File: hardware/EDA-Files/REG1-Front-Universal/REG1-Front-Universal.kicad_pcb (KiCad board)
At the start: 2 copper layers, 15.7 x 43 mm, 10 parts, among them J1 Conn_02x04_Odd_Even, SW1 Prog, SW2 Func, SW5 Res, SW6 BL

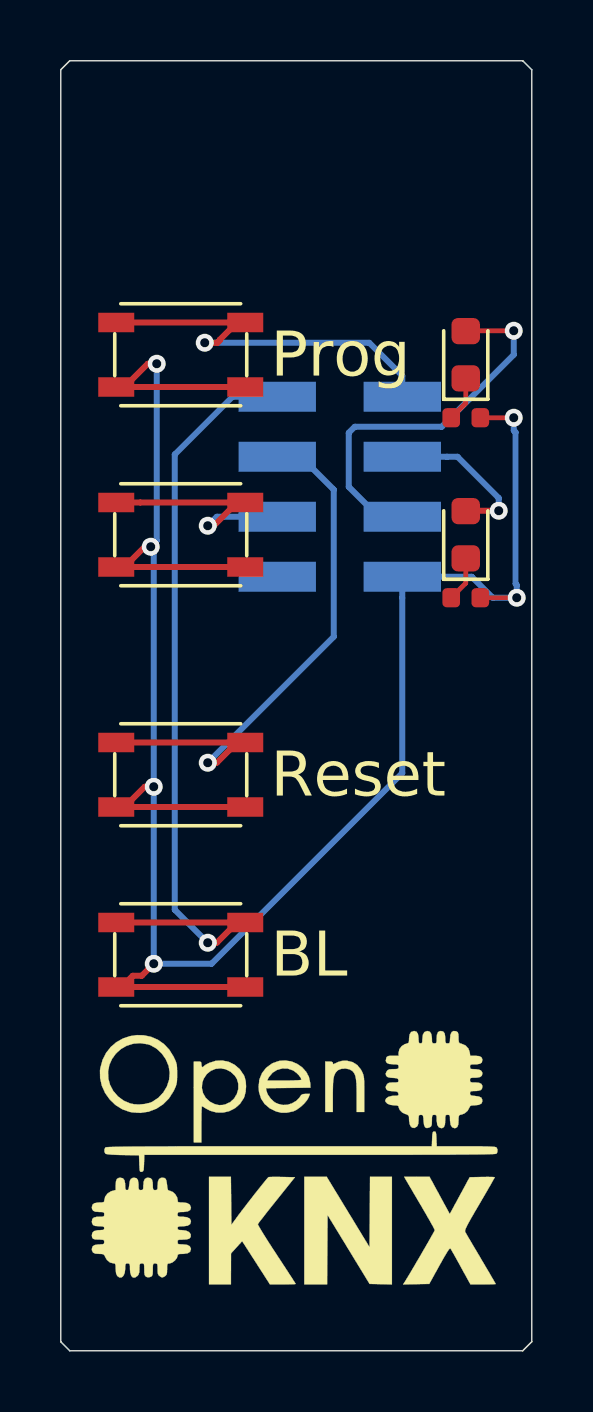
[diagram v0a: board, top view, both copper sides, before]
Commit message: rotate connector, rotate switches, 0.2mm smaller on each side, corrected pinout of connector
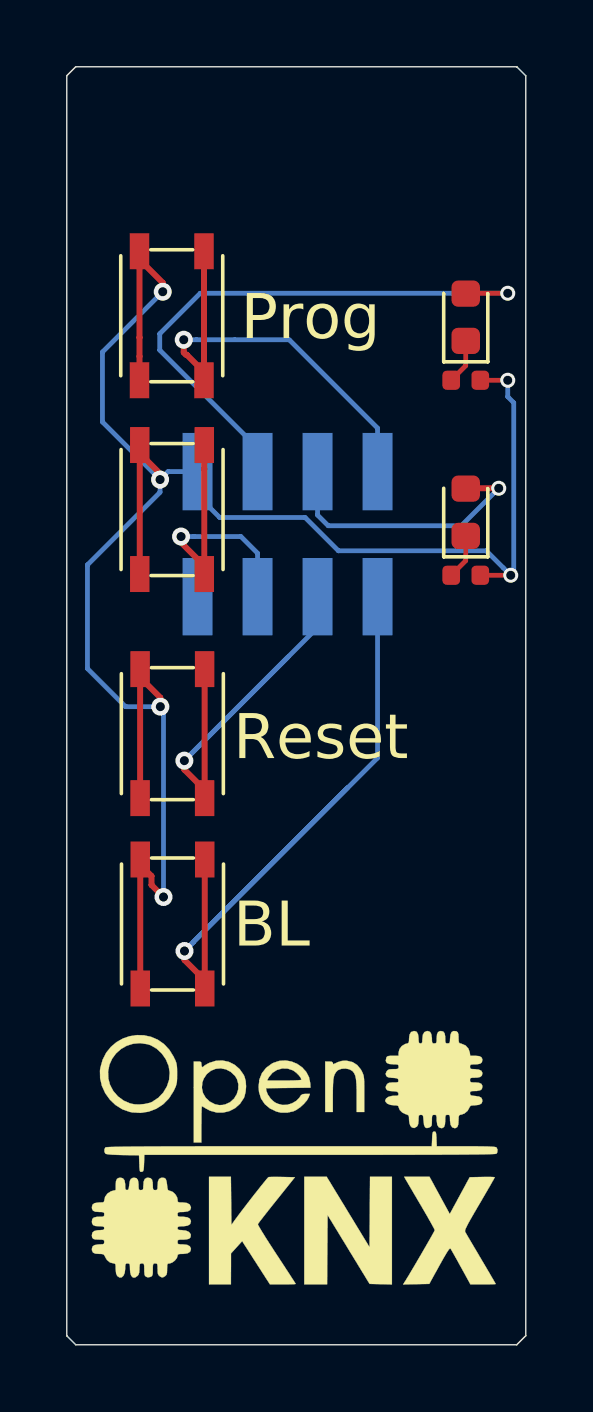
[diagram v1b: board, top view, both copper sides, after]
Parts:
- moved J1 2.35 mm to (105.6, 125.0), turned to 270 degrees
- moved SW3 1.40 mm to (101.7, 131.6), turned to 270 degrees
- moved SW1 1.33 mm to (101.7, 117.7), turned to 270 degrees
- moved D1 1.25 mm to (111.5, 117.8)
- moved R1 1.25 mm to (111.5, 119.8)
- moved SW4 1.06 mm to (101.7, 138.0), turned to 270 degrees
- moved SW2 0.89 mm to (101.7, 124.2), turned to 270 degrees
- moved D2 0.75 mm to (111.5, 124.2)
- moved R2 0.75 mm to (111.5, 126.3)
- renumbered SW5 to SW3, SW6 to SW4
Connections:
- J1 pad 1: +3V3 -> GND
- J1 pad 2: GND -> +3V3
- J1 pad 3: GPIO24 -> PROGLED
- J1 pad 4: PROGLED -> GPIO24
- J1 pad 5: RUN -> GPIO03
- J1 pad 6: GPIO03 -> RUN
- J1 pad 7: BOOTSEL_F -> PROGBTN
- J1 pad 8: PROGBTN -> BOOTSEL_F
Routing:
- net PROGLED: track 13.0 -> 19.5 mm
- net GPIO03: track 5.31 -> 9.26 mm
- net GND: track 73.7 -> 70.5 mm
- net GPIO24: track 8.31 -> 10.1 mm
- net PROGBTN: track 13.7 -> 15.1 mm
- net BOOTSEL_F: track 26.8 -> 28.0 mm
- net RUN: track 19.0 -> 18.0 mm
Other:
- board size 15.7 x 43 mm -> 15.3 x 42.6 mm
- rule via_min_size: 0.6 -> 0.5
- board text added: "REG1-Front-Universal V00.02 © Ing-Dom, 2022"
- board text removed: "REG1-Front-Universal V00.01"
